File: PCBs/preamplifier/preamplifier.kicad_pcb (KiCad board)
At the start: 2 copper layers, 130 x 10.5 mm, 64 parts, among them IC1 LTC6268, IC2 LTC6228, T1 CPH3910, X1 87437-0443

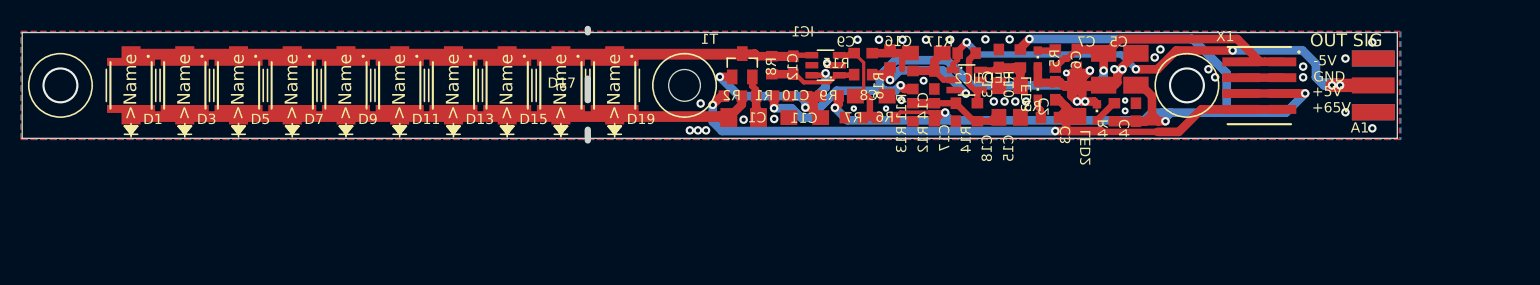
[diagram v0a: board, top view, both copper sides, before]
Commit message: Reorganization of pcb files
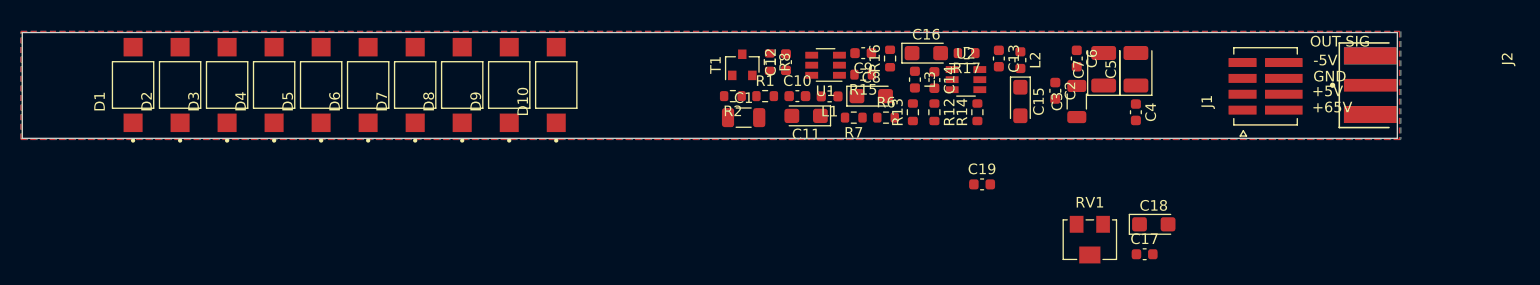
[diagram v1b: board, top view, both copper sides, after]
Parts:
- removed @HOLE0: , 
- removed A1: SMA-EDGE-0.062, preamplifier:CONSMA003.062
- removed D11, D13, D15, D17, D19: VBPW34S, preamplifier:SOD6439X130N
- removed D12, D14, D16, D18, D20: TEMD5010X01, preamplifier:DIODE_TEMD5010
- removed IC1: LTC6268, preamplifier:TSOT23-6
- removed IC2: LTC6228, preamplifier:TSOT23-6
- removed LED1, LED2, LED3: GREEN, preamplifier:CHIPLED_0603
- removed R10, R11, R9: 1, preamplifier:R0603
- removed R3: 43k, preamplifier:R0603
- removed R4, R5: 300, preamplifier:R0603
- removed X1: 87437-0443, preamplifier:87437-0443
- added C19: 10p/50V, Capacitor_SMD:C_0603_1608Metric, F.Cu at (174.2, 114.4)
- added J1: 874370443, semiconductor_radiation_detector:87437-0443, F.Cu at (201.0, 105.2)
- added J2: CON-SMA-EDGE-S, semiconductor_radiation_detector:CON-SMA-EDGE-S, F.Cu at (218.2, 105.1)
- added L1: 1u, Inductor_SMD:L_0603_1608Metric, F.Cu at (159.8, 106.1)
- added L2: 1u, Inductor_SMD:L_0603_1608Metric, F.Cu at (177.9, 102.7)
- added L3: 1u, Inductor_SMD:L_0603_1608Metric, F.Cu at (167.9, 104.5)
- added RV1: 10, Potentiometer_SMD:Potentiometer_Bourns_3224W_Vertical, F.Cu at (184.4, 119.7)
- added U1: LTC6268, Package_TO_SOT_SMD:TSOT-23-6, F.Cu at (159.4, 103.2)
- added U2: LTC6228xS6, Package_TO_SOT_SMD:TSOT-23-6, F.Cu at (172.7, 104.5)
- C1: value 4,7u/50V -> 4,7u/63V; footprint preamplifier:C1206 -> Capacitor_SMD:C_1206_3216Metric
- C10, C12, C13, C14, C17, C2, C4, C6, C9: footprint preamplifier:C0603 -> Capacitor_SMD:C_0603_1608Metric
- C11, C15, C16, C18, C8: footprint preamplifier:SMC_A -> Capacitor_Tantalum_SMD:CP_EIA-3216-18_Kemet-A
- C3: footprint preamplifier:C1206 -> Capacitor_SMD:C_1206_3216Metric
- C5, C7: footprint preamplifier:SMC_B -> Capacitor_Tantalum_SMD:CP_EIA-3528-21_Kemet-B
- D1, D3, D5, D7, D9: footprint preamplifier:SOD6439X130N -> semiconductor_radiation_detector:XDCR_VBPW34S
- D10, D2, D4, D6, D8: value TEMD5010X01 -> VBPW34S; footprint preamplifier:DIODE_TEMD5010 -> semiconductor_radiation_detector:XDCR_VBPW34S
- R1, R12, R14, R15, R16, R17, R2, R6, R7, R8: footprint preamplifier:R0603 -> Resistor_SMD:R_0603_1608Metric
- R13: value 92 -> 100; footprint preamplifier:R0603 -> Resistor_SMD:R_0603_1608Metric
- T1: footprint preamplifier:SOT23 -> Package_TO_SOT_SMD:SOT-23
- moved C17 22.3 mm to (189.6, 121.0), turned to 0 degrees
- moved D10 19.9 mm to (134.0, 105.0)
- moved C18 18.7 mm to (190.5, 118.2), turned to 0 degrees
- moved D8 16.1 mm to (125.1, 105.0)
- moved D9 15.4 mm to (129.5, 105.0)
- moved D6 12.3 mm to (116.2, 105.0)
- moved D7 11.6 mm to (120.7, 105.0)
- moved D4 8.45 mm to (107.3, 105.0)
- moved D5 7.81 mm to (111.8, 105.0)
- moved D2 4.64 mm to (98.4, 105.0)
- moved D3 4.00 mm to (102.9, 105.0)
- moved C12 0.76 mm to (155.7, 102.9)
- moved R8 0.35 mm to (154.2, 102.9), turned to 270 degrees
- moved C11 0.21 mm to (157.6, 108.0)
- moved D1 0.20 mm to (94.0, 105.0)
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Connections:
- C13 pad 2: Net-(C13-Pad2) -> /LTC6268V+
- C14 pad 1: Net-(C14-Pad1) -> /LTC6268V-
- C9 pad 2: Net-(C8-Pad+) -> Net-(C8-Pad1)
- R1 pad 1: -5V -> Net-(C1-Pad2)
- R1 pad 2: Net-(C1-Pad2) -> -5V
- R12 pad 1: Net-(C17-Pad1) -> +5V
- R12 pad 2: +5V -> Net-(R12-Pad2)
- R13 pad 1: GND -> Net-(R13-Pad1)
- R13 pad 2: Net-(C17-Pad1) -> GND
- R14 pad 1: Net-(C17-Pad1) -> Net-(C19-Pad1)
- R14 pad 2: Net-(IC2-Pad4) -> Net-(C17-Pad1)
- R15 pad 1: Net-(IC2-Pad3) -> Net-(C12-Pad1)
- R15 pad 2: Net-(C12-Pad1) -> Net-(R15-Pad2)
- R16 pad 1: Net-(IC2-Pad3) -> Net-(R15-Pad2)
- R17 pad 1: Net-(IC2-Pad4) -> Net-(C19-Pad2)
- R17 pad 2: Net-(A1-PadANT) -> Net-(C19-Pad1)
- R2 pad 1: /+65V -> Net-(C1-Pad1)
- R2 pad 2: Net-(C1-Pad1) -> (no net)
- R6 pad 1: Net-(C8-Pad+) -> +5V
- R6 pad 2: +5V -> Net-(C8-Pad1)
- R7 pad 1: GND -> Net-(C8-Pad1)
- R7 pad 2: Net-(C8-Pad+) -> GND
- R8 pad 1: Net-(C12-Pad1) -> Net-(C12-Pad2)
- R8 pad 2: Net-(C12-Pad2) -> Net-(C12-Pad1)
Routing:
- net +5V: track 107.4 -> 0.00 mm, vias 5 -> 0
- net Net-(C12-Pad2): track 75.8 -> 0.00 mm
- net -5V: track 69.3 -> 0.00 mm, vias 3 -> 0
- net /+65V: track 66.5 -> 0.00 mm, vias 2 -> 0
- net Net-(C1-Pad1): track 66.5 -> 0.00 mm
- net Net-(A1-PadANT): track 49.3 -> 0.00 mm, vias 5 -> 0
- net GND: track 38.0 -> 0.00 mm, vias 41 -> 0
- net /LOC+5V: track 22.9 -> 0.00 mm, vias 3 -> 0
- net Net-(C12-Pad1): track 13.9 -> 0.00 mm
- net Net-(IC2-Pad3): track 13.6 -> 0.00 mm, vias 2 -> 0
- net Net-(C8-Pad+): track 12.6 -> 0.00 mm
- net Net-(C17-Pad1): track 9.99 -> 0.00 mm
- net Net-(C14-Pad1): track 6.13 -> 0.00 mm
- net Net-(C13-Pad2): track 5.80 -> 0.00 mm
- net Net-(IC2-Pad4): track 5.72 -> 0.00 mm
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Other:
- board size 130 x 10.5 mm -> 130 x 10 mm
- board text added: "Semiconductor radiation detector: preamplifier Marcin Wachowiak, Poland"
- board text added: "optional cut"
- board text removed: "GAMMA PIN semiconductor radiation detector: Preamplifier Marcin Wachowiak, Poland 2.11.2019"
- board text removed: "cut"
- board text removed: "optional"

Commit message: finished preamplifier board redesigning
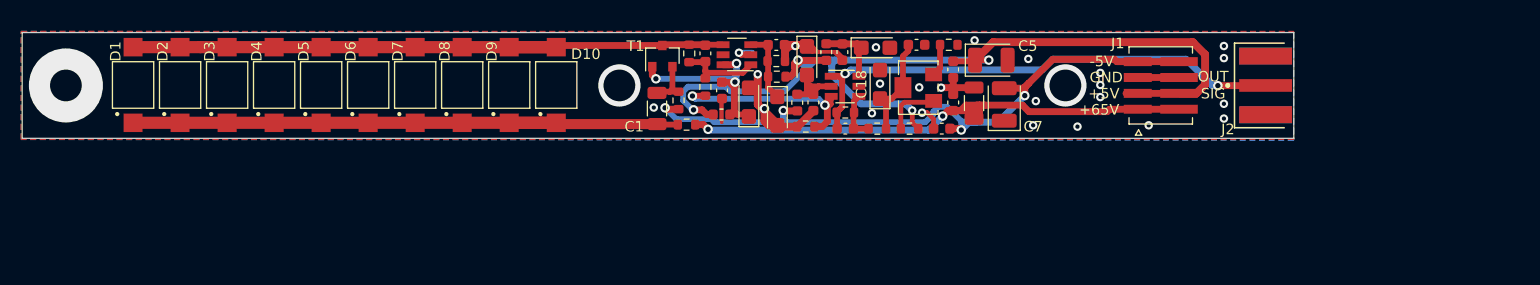
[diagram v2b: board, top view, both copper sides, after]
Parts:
- moved C17 29.3 mm to (168.0, 101.2)
- moved C18 29.1 mm to (164.6, 105.0), turned to 90 degrees
- moved RV1 21.7 mm to (168.2, 105.3), turned to 270 degrees
- moved L2 18.4 mm to (159.5, 101.9), turned to 90 degrees
- moved C4 17.7 mm to (171.5, 103.6), turned to 90 degrees
- moved R15 15.0 mm to (148.1, 105.2), turned to 270 degrees
- moved C13 14.8 mm to (161.0, 101.9), turned to 90 degrees
- moved C15 14.6 mm to (164.2, 101.5), turned to 0 degrees
- moved C6 14.4 mm to (170.4, 109.2), turned to 180 degrees
- moved C19 14.0 mm to (161.3, 109.2), turned to 180 degrees
- moved C5 13.7 mm to (175.1, 102.7), turned to 0 degrees
- moved R17 12.8 mm to (161.3, 107.6), turned to 0 degrees
- moved C14 11.6 mm to (158.3, 106.7)
- moved U2 11.4 mm to (161.3, 105.2)
- moved L3 11.3 mm to (156.8, 106.7)
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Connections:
- C2 pad 2: /+65V -> /+60V
- C3 pad 1: /+65V -> /+60V
- J1 pad 1_1: /+65V -> /+60V
- J1 pad 1_2: /+65V -> /+60V
- R2 pad 2: (no net) -> /+60V
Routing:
- net +5V: track 0.00 -> 94.6 mm, vias 0 -> 4
- net -5V: track 0.00 -> 66.5 mm, vias 0 -> 4
- net Net-(C12-Pad2): track 0.00 -> 60.5 mm
- net /+60V: track 0.00 -> 57.8 mm, vias 0 -> 2
- net Net-(C1-Pad1): track 0.00 -> 56.0 mm
- net Net-(C19-Pad2): track 0.00 -> 50.6 mm, vias 0 -> 2
- net GND: track 0.00 -> 41.6 mm, vias 0 -> 24
- net /LOC+5V: track 0.00 -> 28.3 mm, vias 0 -> 3
- net Net-(R15-Pad2): track 0.00 -> 20.9 mm, vias 0 -> 2
- net Net-(C17-Pad1): track 0.00 -> 10.9 mm
- net Net-(C12-Pad1): track 0.00 -> 7.67 mm
- net /LTC6268V-: track 0.00 -> 7.34 mm
- net Net-(C8-Pad1): track 0.00 -> 6.91 mm
- net /LTC6268V+: track 0.00 -> 6.26 mm
- net Net-(R12-Pad2): track 0.00 -> 5.76 mm
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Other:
- board size 130 x 10 mm -> 120.2 x 10 mm
